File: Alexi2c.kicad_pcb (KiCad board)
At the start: 2 copper layers, 50 x 100 mm, 26 parts, among them J1 Conn_01x04, J10 Conn_01x01, J11 Conn_01x09, J12 Conn_01x02, J13 Conn_01x02, J2 Conn_02x03_Counter_Clockwise, J3 Conn_01x02, J4 Conn_01x10, J5 Conn_01x10, J6 Conn_01x09, J7 Conn_01x01, J8 Conn_01x01, J9 Conn_01x01, U1 78M05, U2 TCA9555PWR, U3 ULN2803A, U4 ULN2803A

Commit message: Readme cleanup
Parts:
- J12, J13: footprint conn_kk100:kk100_22-23-2021 -> Pin_Headers:Pin_Header_Straight_1x02_Pitch2.54mm
- moved J12 1.27 mm to (137.8, 116.2), turned to 0 degrees
- moved J13 1.27 mm to (137.8, 51.2), turned to 0 degrees

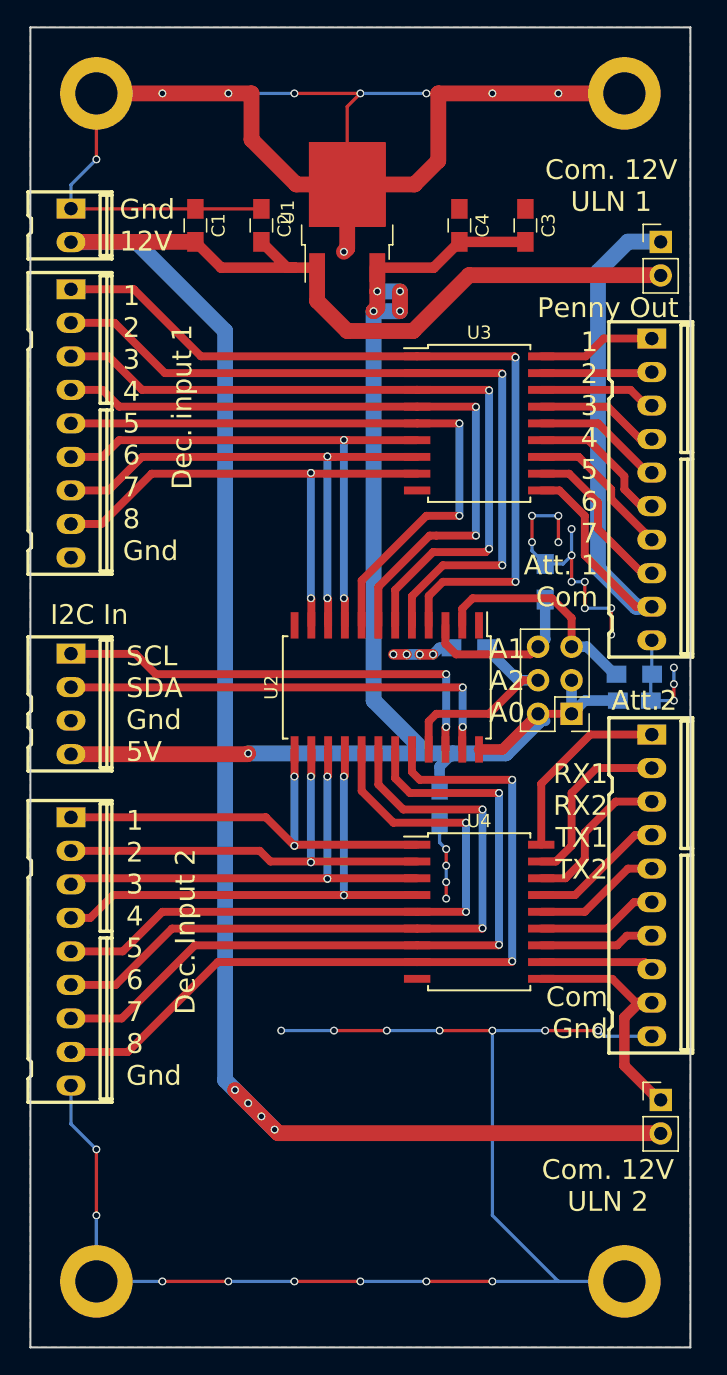
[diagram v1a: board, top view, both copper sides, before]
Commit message: new I2C decoder module
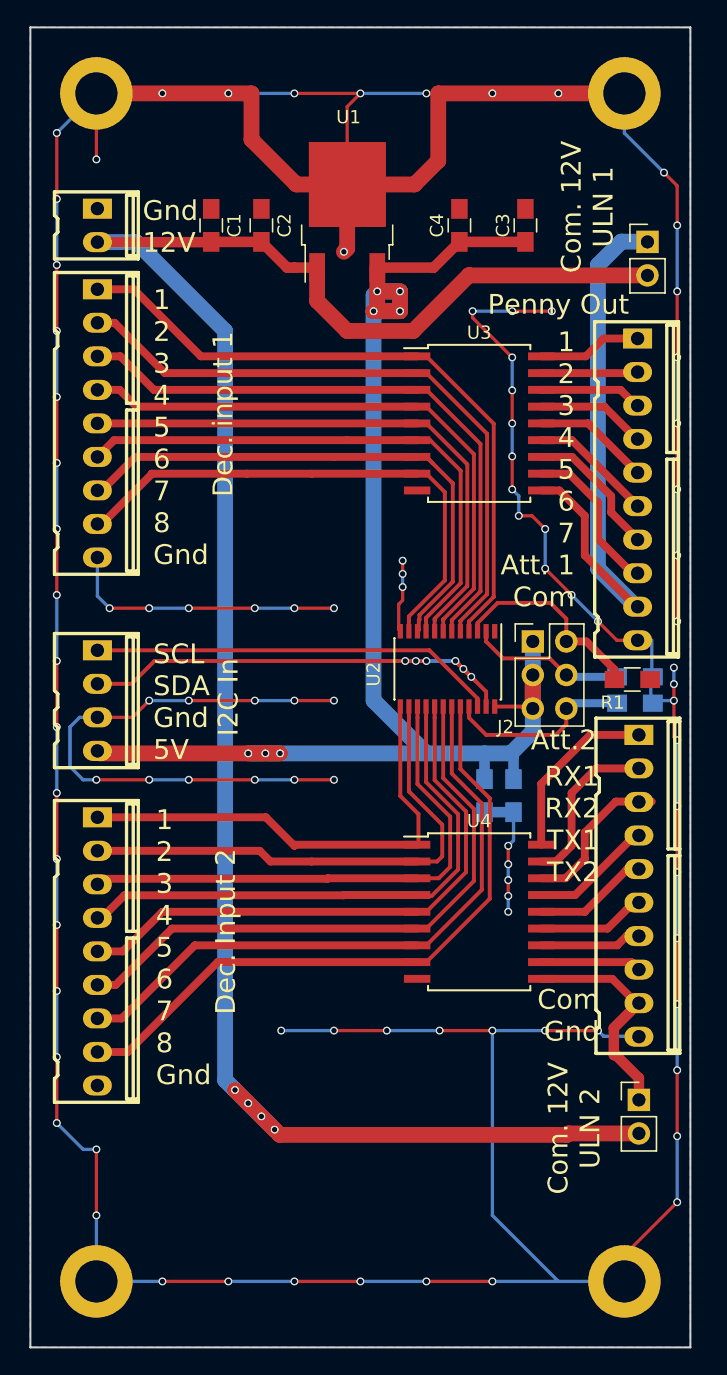
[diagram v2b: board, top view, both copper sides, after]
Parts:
- J2: value Conn_02x03_Counter_Clockwise -> Conn_02x03_Odd_Even
- R1: moved to F.Cu
- U2: footprint Housings_SOIC:SOIC-24W_7.5x15.4mm_Pitch1.27mm -> Housings_SSOP:TSSOP-24_4.4x7.8mm_Pitch0.65mm
- moved C6 13.4 mm to (124.4, 93.2), turned to 90 degrees
- moved R3 13.2 mm to (135.8, 86.2), turned to 0 degrees
- moved R1 9.92 mm to (135.6, 84.4), turned to 0 degrees
- moved J2 6.22 mm to (128.1, 81.5), turned to 0 degrees
- moved C5 5.66 mm to (126.6, 93.2)
- moved U2 4.81 mm to (121.6, 83.6)
- moved J1 2.02 mm to (95.0, 86.0)
- moved J11 2.00 mm to (95.0, 105.0)
- moved J3 2.00 mm to (95.0, 50.0)
- moved J6 2.00 mm to (95.0, 65.0)
- moved J12 1.65 mm to (136.1, 116.2)
- moved C1 1.20 mm to (103.7, 50.0)
- moved J4 1.08 mm to (135.9, 70.0)
- moved J13 1.00 mm to (136.8, 51.2)
- moved J5 0.98 mm to (136.0, 100.0)
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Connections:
- J2 pad 2: Net-(C3-Pad2) -> Net-(J2-Pad2)
- J2 pad 5: Net-(J2-Pad5) -> Net-(C3-Pad2)
- R1 pad 1: Net-(J2-Pad6) -> Net-(J2-Pad2)
- R2 pad 1: Net-(J2-Pad5) -> Net-(J2-Pad4)
- R3 pad 1: Net-(J2-Pad4) -> Net-(J2-Pad6)
- U2 pad 2: Net-(J2-Pad5) -> Net-(J2-Pad4)
- U2 pad 21: Net-(J2-Pad4) -> Net-(J2-Pad6)
- U2 pad 3: Net-(J2-Pad6) -> Net-(J2-Pad2)
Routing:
- net GND: track 272.9 -> 505.5 mm, vias 46 -> 97
- net Net-(J2-Pad5): track 16.9 -> 0.00 mm
- net Net-(J2-Pad2): track 0.00 -> 15.5 mm
- net Net-(J6-Pad1): track 62.1 -> 50.7 mm, vias 2 -> 0
- net Net-(J6-Pad2): track 58.8 -> 48.8 mm, vias 2 -> 0
- net Net-(J11-Pad8): track 59.6 -> 50.0 mm, vias 2 -> 0
- net Net-(C1-Pad2): track 165.7 -> 156.2 mm
- net Net-(J6-Pad3): track 55.8 -> 46.9 mm, vias 2 -> 0
- net Net-(J11-Pad7): track 56.7 -> 48.0 mm, vias 2 -> 0
- net Net-(J6-Pad4): track 52.9 -> 44.9 mm, vias 2 -> 0
- net Net-(J11-Pad6): track 53.3 -> 46.0 mm, vias 2 -> 0
- net Net-(J6-Pad5): track 49.3 -> 43.0 mm, vias 2 -> 0
- net Net-(J11-Pad5): track 50.0 -> 43.9 mm, vias 2 -> 0
- net Net-(J2-Pad4): track 16.6 -> 11.8 mm
- net Net-(J11-Pad4): track 38.3 -> 43.0 mm, vias 2 -> 0
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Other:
- board text added: "30/20m 60/ 40m 80m 160m 6m 12/10m 17/15m Alex LPF"
- board text removed: "30/20m 60/40m 80m 160m 6m 12/10m 17/15m Alex LPF"

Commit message: added protec. diode, I2C Pull-up, I2C Vdd strap
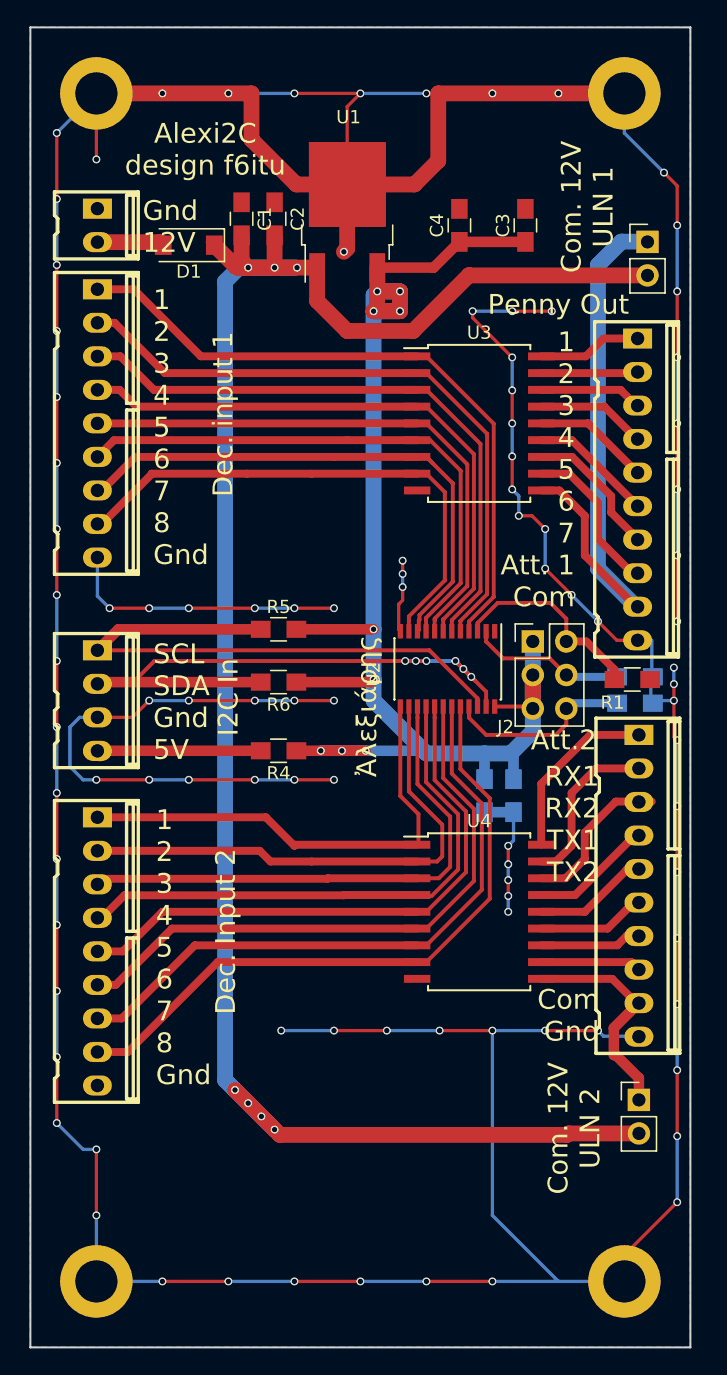
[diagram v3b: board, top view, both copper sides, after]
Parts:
- added D1: D, Diodes_SMD:D_2010, F.Cu at (102.0, 51.5)
- added R4: 0R, Resistors_SMD:R_0805_HandSoldering, F.Cu at (108.8, 89.8)
- added R5: 4k7, Resistors_SMD:R_0805_HandSoldering, F.Cu at (108.8, 80.6)
- added R6: 4k7, Resistors_SMD:R_0805_HandSoldering, F.Cu at (108.8, 84.6)
- moved C1 2.35 mm to (106.0, 49.5)
- moved C2 1.12 mm to (108.5, 49.5)
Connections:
- J1 pad 4: Net-(C3-Pad2) -> Net-(J1-Pad4)
- J3 pad 2: Net-(C1-Pad2) -> Net-(D1-Pad2)
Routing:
- net Net-(J1-Pad1): track 30.9 -> 44.0 mm
- net Net-(J1-Pad4): track 0.00 -> 12.9 mm
- net Net-(J1-Pad2): track 37.2 -> 50.0 mm
- net Net-(C1-Pad2): track 156.2 -> 150.0 mm, vias 4 -> 7
- net Net-(D1-Pad2): track 0.00 -> 5.08 mm
- net Net-(C3-Pad2): track 116.1 -> 113.8 mm, vias 7 -> 9
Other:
- board text added: "Alexi2C design f6itu"
- board text added: "Ἀλεξιάρης"

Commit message: image and BOM added, minor changes
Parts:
- removed C1: 100n, Capacitors_SMD:C_0805_HandSoldering
- removed C2: 1u, Capacitors_SMD:C_0805_HandSoldering
- removed C3, C4: C, Capacitors_SMD:C_0805_HandSoldering
- removed U1: 78M05, TO_SOT_Packages_SMD:TO-252-2
- added R7: 4k7, Resistors_SMD:R_0805_HandSoldering, F.Cu at (125.4, 77.0)
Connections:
- U2 pad 1: (no net) -> Net-(R7-Pad2)
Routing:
- net GND: track 505.5 -> 442.9 mm, vias 97 -> 96
- net Net-(C5-Pad2): track 113.8 -> 67.6 mm, vias 9 -> 4
- net Net-(D1-Pad1): track 150.0 -> 138.9 mm
- net Net-(J2-Pad2): track 15.5 -> 24.1 mm
- net Net-(R7-Pad2): track 0.00 -> 4.29 mm
- net Net-(J6-Pad6): track 42.3 -> 41.6 mm
- net Net-(J6-Pad8): track 40.2 -> 39.6 mm
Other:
- board text added: "1 2 3 4 5 6 7 Att1 Com"
- board text added: "Alexi2C f6itu"
- board text added: "Alexi2C Ἄλεξις Alexiares emulation interface"
- board text added: "Att2"
- board text removed: "1 2 3 4 5 6 7 Att. 1 Com"
- board text removed: "Alexi2C design f6itu"
- board text removed: "Att.2"

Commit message: new stitching, minor silkmask mods
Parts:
- added REF**: via, via:via, F.Cu at (139.0, 50.0)
- added REF**: via, via:via, F.Cu at (139.0, 63.5)
- added REF**: via, via:via, F.Cu at (91.0, 91.5)
- added REF**: via, via:via, F.Cu at (92.5, 90.0)
- added REF**: via, via:via, F.Cu at (91.0, 90.0)
- added REF**: via, via:via, F.Cu at (92.5, 88.5)
- added REF**: via, via:via, F.Cu at (91.0, 88.5)
- added REF**: via, via:via, F.Cu at (92.5, 87.0)
- added REF**: via, via:via, F.Cu at (91.0, 87.0)
- added REF**: via, via:via, F.Cu at (92.5, 85.5)
- added REF**: via, via:via, F.Cu at (91.0, 85.5)
- added REF**: via, via:via, F.Cu at (92.5, 84.0)
- added REF**: via, via:via, F.Cu at (139.0, 65.0)
- added REF**: via, via:via, F.Cu at (91.0, 84.0)
- added REF**: via, via:via, F.Cu at (92.5, 82.5)
- added REF**: via, via:via, F.Cu at (91.0, 82.5)
- added REF**: via, via:via, F.Cu at (92.5, 81.0)
- added REF**: via, via:via, F.Cu at (91.0, 81.0)
- added REF**: via, via:via, F.Cu at (92.5, 79.5)
- added REF**: via, via:via, F.Cu at (91.0, 79.5)
- added REF**: via, via:via, F.Cu at (92.5, 78.0)
- added REF**: via, via:via, F.Cu at (91.0, 78.0)
- added REF**: via, via:via, F.Cu at (92.5, 76.5)
- added REF**: via, via:via, F.Cu at (139.0, 66.5)
- added REF**: via, via:via, F.Cu at (91.0, 76.5)
- added REF**: via, via:via, F.Cu at (92.5, 75.0)
- added REF**: via, via:via, F.Cu at (91.0, 75.0)
- added REF**: via, via:via, F.Cu at (92.5, 73.5)
- added REF**: via, via:via, F.Cu at (91.0, 73.5)
- added REF**: via, via:via, F.Cu at (92.5, 72.0)
- added REF**: via, via:via, F.Cu at (91.0, 72.0)
- added REF**: via, via:via, F.Cu at (92.5, 70.5)
- added REF**: via, via:via, F.Cu at (91.0, 70.5)
- added REF**: via, via:via, F.Cu at (92.5, 69.0)
- added REF**: via, via:via, F.Cu at (139.0, 68.0)
- added REF**: via, via:via, F.Cu at (91.0, 69.0)
- added REF**: via, via:via, F.Cu at (92.5, 67.5)
- added REF**: via, via:via, F.Cu at (91.0, 67.5)
- added REF**: via, via:via, F.Cu at (92.5, 66.0)
- added REF**: via, via:via, F.Cu at (91.0, 66.0)
- added REF**: via, via:via, F.Cu at (92.5, 64.5)
- added REF**: via, via:via, F.Cu at (91.0, 64.5)
- added REF**: via, via:via, F.Cu at (92.5, 63.0)
- added REF**: via, via:via, F.Cu at (91.0, 63.0)
- added REF**: via, via:via, F.Cu at (92.5, 61.5)
- added REF**: via, via:via, F.Cu at (139.0, 69.5)
- added REF**: via, via:via, F.Cu at (91.0, 61.5)
- added REF**: via, via:via, F.Cu at (92.5, 60.0)
- added REF**: via, via:via, F.Cu at (91.0, 60.0)
- added REF**: via, via:via, F.Cu at (92.5, 58.5)
- added REF**: via, via:via, F.Cu at (91.0, 58.5)
- added REF**: via, via:via, F.Cu at (92.5, 57.0)
- added REF**: via, via:via, F.Cu at (91.0, 57.0)
- added REF**: via, via:via, F.Cu at (92.5, 55.5)
- added REF**: via, via:via, F.Cu at (91.0, 55.5)
- added REF**: via, via:via, F.Cu at (92.5, 54.0)
- added REF**: via, via:via, F.Cu at (139.0, 71.0)
- added REF**: via, via:via, F.Cu at (91.0, 54.0)
- added REF**: via, via:via, F.Cu at (92.5, 52.5)
- added REF**: via, via:via, F.Cu at (91.0, 52.5)
- added REF**: via, via:via, F.Cu at (92.5, 51.0)
- added REF**: via, via:via, F.Cu at (91.0, 51.0)
- added REF**: via, via:via, F.Cu at (92.5, 49.5)
- added REF**: via, via:via, F.Cu at (91.0, 49.5)
- added REF**: via, via:via, F.Cu at (92.5, 48.0)
- added REF**: via, via:via, F.Cu at (91.0, 48.0)
- added REF**: via, via:via, F.Cu at (92.5, 46.5)
- added REF**: via, via:via, F.Cu at (139.0, 72.5)
- added REF**: via, via:via, F.Cu at (91.0, 46.5)
- added REF**: via, via:via, F.Cu at (92.5, 45.0)
- added REF**: via, via:via, F.Cu at (91.0, 45.0)
- added REF**: via, via:via, F.Cu at (103.0, 76.5)
- added REF**: via, via:via, F.Cu at (101.5, 76.5)
- added REF**: via, via:via, F.Cu at (100.0, 76.5)
- added REF**: via, via:via, F.Cu at (103.0, 75.0)
- added REF**: via, via:via, F.Cu at (101.5, 75.0)
- added REF**: via, via:via, F.Cu at (100.0, 75.0)
- added REF**: via, via:via, F.Cu at (103.0, 73.5)
- added REF**: via, via:via, F.Cu at (139.0, 74.0)
- added REF**: via, via:via, F.Cu at (101.5, 73.5)
- added REF**: via, via:via, F.Cu at (100.0, 73.5)
- added REF**: via, via:via, F.Cu at (103.0, 72.0)
- added REF**: via, via:via, F.Cu at (101.5, 72.0)
- added REF**: via, via:via, F.Cu at (100.0, 72.0)
- added REF**: via, via:via, F.Cu at (108.5, 72.0)
- added REF**: via, via:via, F.Cu at (110.0, 72.0)
- added REF**: via, via:via, F.Cu at (111.5, 72.0)
- added REF**: via, via:via, F.Cu at (113.0, 72.0)
- added REF**: via, via:via, F.Cu at (114.5, 72.0)
- added REF**: via, via:via, F.Cu at (139.0, 75.5)
- added REF**: via, via:via, F.Cu at (116.0, 72.0)
- added REF**: via, via:via, F.Cu at (108.5, 73.5)
- added REF**: via, via:via, F.Cu at (110.0, 73.5)
- added REF**: via, via:via, F.Cu at (111.5, 73.5)
- added REF**: via, via:via, F.Cu at (113.0, 73.5)
- added REF**: via, via:via, F.Cu at (114.5, 73.5)
- added REF**: via, via:via, F.Cu at (116.0, 73.5)
- added REF**: via, via:via, F.Cu at (108.5, 75.0)
- added REF**: via, via:via, F.Cu at (110.0, 75.0)
- added REF**: via, via:via, F.Cu at (111.5, 75.0)
- added REF**: via, via:via, F.Cu at (139.0, 77.0)
- added REF**: via, via:via, F.Cu at (113.0, 75.0)
- added REF**: via, via:via, F.Cu at (114.5, 75.0)
- added REF**: via, via:via, F.Cu at (116.0, 75.0)
- added REF**: via, via:via, F.Cu at (108.5, 76.5)
- added REF**: via, via:via, F.Cu at (110.0, 76.5)
- added REF**: via, via:via, F.Cu at (111.5, 76.5)
- added REF**: via, via:via, F.Cu at (113.0, 76.5)
- added REF**: via, via:via, F.Cu at (114.5, 76.5)
- added REF**: via, via:via, F.Cu at (116.0, 76.5)
- added REF**: via, via:via, F.Cu at (102.5, 93.5)
- added REF**: via, via:via, F.Cu at (139.0, 51.5)
- added REF**: via, via:via, F.Cu at (139.0, 78.5)
- added REF**: via, via:via, F.Cu at (101.0, 93.5)
- added REF**: via, via:via, F.Cu at (99.5, 93.5)
- added REF**: via, via:via, F.Cu at (102.5, 92.0)
- added REF**: via, via:via, F.Cu at (101.0, 92.0)
- added REF**: via, via:via, F.Cu at (99.5, 92.0)
- added REF**: via, via:via, F.Cu at (107.5, 92.0)
- added REF**: via, via:via, F.Cu at (109.0, 92.0)
- added REF**: via, via:via, F.Cu at (110.5, 92.0)
- added REF**: via, via:via, F.Cu at (112.0, 92.0)
- added REF**: via, via:via, F.Cu at (113.5, 92.0)
- added REF**: via, via:via, F.Cu at (139.0, 80.0)
- added REF**: via, via:via, F.Cu at (115.0, 92.0)
- added REF**: via, via:via, F.Cu at (116.5, 92.0)
- added REF**: via, via:via, F.Cu at (107.5, 93.5)
- added REF**: via, via:via, F.Cu at (109.0, 93.5)
- added REF**: via, via:via, F.Cu at (110.5, 93.5)
- added REF**: via, via:via, F.Cu at (112.0, 93.5)
- added REF**: via, via:via, F.Cu at (113.5, 93.5)
- added REF**: via, via:via, F.Cu at (115.0, 93.5)
- added REF**: via, via:via, F.Cu at (116.5, 93.5)
- added REF**: via, via:via, F.Cu at (128.5, 115.0)
- added REF**: via, via:via, F.Cu at (139.0, 81.5)
- added REF**: via, via:via, F.Cu at (127.0, 115.0)
- added REF**: via, via:via, F.Cu at (125.5, 115.0)
- added REF**: via, via:via, F.Cu at (124.0, 115.0)
- added REF**: via, via:via, F.Cu at (122.5, 115.0)
- added REF**: via, via:via, F.Cu at (121.0, 115.0)
- added REF**: via, via:via, F.Cu at (119.5, 115.0)
- added REF**: via, via:via, F.Cu at (118.0, 115.0)
- added REF**: via, via:via, F.Cu at (116.5, 115.0)
- added REF**: via, via:via, F.Cu at (115.0, 115.0)
- added REF**: via, via:via, F.Cu at (113.5, 115.0)
- added REF**: via, via:via, F.Cu at (139.0, 83.0)
- added REF**: via, via:via, F.Cu at (112.0, 115.0)
- added REF**: via, via:via, F.Cu at (110.5, 115.0)
- added REF**: via, via:via, F.Cu at (109.0, 115.0)
- added REF**: via, via:via, F.Cu at (128.5, 113.5)
- added REF**: via, via:via, F.Cu at (127.0, 113.5)
- added REF**: via, via:via, F.Cu at (125.5, 113.5)
- added REF**: via, via:via, F.Cu at (124.0, 113.5)
- added REF**: via, via:via, F.Cu at (122.5, 113.5)
- added REF**: via, via:via, F.Cu at (121.0, 113.5)
- added REF**: via, via:via, F.Cu at (119.5, 113.5)
- added REF**: via, via:via, F.Cu at (139.0, 84.5)
- added REF**: via, via:via, F.Cu at (118.0, 113.5)
- added REF**: via, via:via, F.Cu at (116.5, 113.5)
- added REF**: via, via:via, F.Cu at (115.0, 113.5)
- added REF**: via, via:via, F.Cu at (113.5, 113.5)
- added REF**: via, via:via, F.Cu at (112.0, 113.5)
- added REF**: via, via:via, F.Cu at (110.5, 113.5)
- added REF**: via, via:via, F.Cu at (109.0, 113.5)
- added REF**: via, via:via, F.Cu at (128.5, 112.0)
- added REF**: via, via:via, F.Cu at (127.0, 112.0)
- added REF**: via, via:via, F.Cu at (125.5, 112.0)
- added REF**: via, via:via, F.Cu at (139.0, 86.0)
- added REF**: via, via:via, F.Cu at (124.0, 112.0)
- added REF**: via, via:via, F.Cu at (122.5, 112.0)
- added REF**: via, via:via, F.Cu at (121.0, 112.0)
- added REF**: via, via:via, F.Cu at (119.5, 112.0)
- added REF**: via, via:via, F.Cu at (118.0, 112.0)
- added REF**: via, via:via, F.Cu at (116.5, 112.0)
- added REF**: via, via:via, F.Cu at (115.0, 112.0)
- added REF**: via, via:via, F.Cu at (113.5, 112.0)
- added REF**: via, via:via, F.Cu at (112.0, 112.0)
- added REF**: via, via:via, F.Cu at (110.5, 112.0)
- added REF**: via, via:via, F.Cu at (139.0, 87.5)
- added REF**: via, via:via, F.Cu at (109.0, 112.0)
- added REF**: via, via:via, F.Cu at (128.5, 110.5)
- added REF**: via, via:via, F.Cu at (127.0, 110.5)
- added REF**: via, via:via, F.Cu at (125.5, 110.5)
- added REF**: via, via:via, F.Cu at (124.0, 110.5)
- added REF**: via, via:via, F.Cu at (122.5, 110.5)
- added REF**: via, via:via, F.Cu at (121.0, 110.5)
- added REF**: via, via:via, F.Cu at (119.5, 110.5)
- added REF**: via, via:via, F.Cu at (118.0, 110.5)
- added REF**: via, via:via, F.Cu at (116.5, 110.5)
- added REF**: via, via:via, F.Cu at (139.0, 89.0)
- added REF**: via, via:via, F.Cu at (115.0, 110.5)
- added REF**: via, via:via, F.Cu at (113.5, 110.5)
- added REF**: via, via:via, F.Cu at (112.0, 110.5)
- added REF**: via, via:via, F.Cu at (110.5, 110.5)
- added REF**: via, via:via, F.Cu at (109.0, 110.5)
- added REF**: via, via:via, F.Cu at (99.0, 129.0)
- added REF**: via, via:via, F.Cu at (100.5, 129.0)
- added REF**: via, via:via, F.Cu at (102.0, 129.0)
- added REF**: via, via:via, F.Cu at (103.5, 129.0)
- added REF**: via, via:via, F.Cu at (105.0, 129.0)
- added REF**: via, via:via, F.Cu at (139.0, 90.5)
- added REF**: via, via:via, F.Cu at (106.5, 129.0)
- added REF**: via, via:via, F.Cu at (108.0, 129.0)
- added REF**: via, via:via, F.Cu at (109.5, 129.0)
- added REF**: via, via:via, F.Cu at (111.0, 129.0)
- added REF**: via, via:via, F.Cu at (112.5, 129.0)
- added REF**: via, via:via, F.Cu at (114.0, 129.0)
- added REF**: via, via:via, F.Cu at (115.5, 129.0)
- added REF**: via, via:via, F.Cu at (117.0, 129.0)
- added REF**: via, via:via, F.Cu at (118.5, 129.0)
- added REF**: via, via:via, F.Cu at (120.0, 129.0)
- added REF**: via, via:via, F.Cu at (139.0, 92.0)
- added REF**: via, via:via, F.Cu at (121.5, 129.0)
- added REF**: via, via:via, F.Cu at (123.0, 129.0)
- added REF**: via, via:via, F.Cu at (124.5, 129.0)
- added REF**: via, via:via, F.Cu at (126.0, 129.0)
- added REF**: via, via:via, F.Cu at (127.5, 129.0)
- added REF**: via, via:via, F.Cu at (129.0, 129.0)
- added REF**: via, via:via, F.Cu at (130.5, 129.0)
- added REF**: via, via:via, F.Cu at (99.0, 130.5)
- added REF**: via, via:via, F.Cu at (100.5, 130.5)
- added REF**: via, via:via, F.Cu at (102.0, 130.5)
- added REF**: via, via:via, F.Cu at (139.0, 53.0)
- added REF**: via, via:via, F.Cu at (139.0, 93.5)
- added REF**: via, via:via, F.Cu at (103.5, 130.5)
- added REF**: via, via:via, F.Cu at (105.0, 130.5)
- added REF**: via, via:via, F.Cu at (106.5, 130.5)
- added REF**: via, via:via, F.Cu at (108.0, 130.5)
- added REF**: via, via:via, F.Cu at (109.5, 130.5)
- added REF**: via, via:via, F.Cu at (111.0, 130.5)
- added REF**: via, via:via, F.Cu at (112.5, 130.5)
- added REF**: via, via:via, F.Cu at (114.0, 130.5)
- added REF**: via, via:via, F.Cu at (115.5, 130.5)
- added REF**: via, via:via, F.Cu at (117.0, 130.5)
- added REF**: via, via:via, F.Cu at (139.0, 95.0)
- added REF**: via, via:via, F.Cu at (118.5, 130.5)
- added REF**: via, via:via, F.Cu at (120.0, 130.5)
- added REF**: via, via:via, F.Cu at (121.5, 130.5)
- added REF**: via, via:via, F.Cu at (123.0, 130.5)
- added REF**: via, via:via, F.Cu at (124.5, 130.5)
- added REF**: via, via:via, F.Cu at (126.0, 130.5)
- added REF**: via, via:via, F.Cu at (127.5, 130.5)
- added REF**: via, via:via, F.Cu at (129.0, 130.5)
- added REF**: via, via:via, F.Cu at (130.5, 130.5)
- added REF**: via, via:via, F.Cu at (99.0, 132.0)
- added REF**: via, via:via, F.Cu at (139.0, 96.5)
- added REF**: via, via:via, F.Cu at (100.5, 132.0)
- added REF**: via, via:via, F.Cu at (102.0, 132.0)
- added REF**: via, via:via, F.Cu at (103.5, 132.0)
- added REF**: via, via:via, F.Cu at (105.0, 132.0)
- added REF**: via, via:via, F.Cu at (106.5, 132.0)
- added REF**: via, via:via, F.Cu at (108.0, 132.0)
- added REF**: via, via:via, F.Cu at (109.5, 132.0)
- added REF**: via, via:via, F.Cu at (111.0, 132.0)
- added REF**: via, via:via, F.Cu at (112.5, 132.0)
- added REF**: via, via:via, F.Cu at (114.0, 132.0)
- added REF**: via, via:via, F.Cu at (139.0, 98.0)
- added REF**: via, via:via, F.Cu at (115.5, 132.0)
- added REF**: via, via:via, F.Cu at (117.0, 132.0)
- added REF**: via, via:via, F.Cu at (118.5, 132.0)
- added REF**: via, via:via, F.Cu at (120.0, 132.0)
- added REF**: via, via:via, F.Cu at (121.5, 132.0)
- added REF**: via, via:via, F.Cu at (123.0, 132.0)
- added REF**: via, via:via, F.Cu at (124.5, 132.0)
- added REF**: via, via:via, F.Cu at (126.0, 132.0)
- added REF**: via, via:via, F.Cu at (127.5, 132.0)
- added REF**: via, via:via, F.Cu at (129.0, 132.0)
- added REF**: via, via:via, F.Cu at (139.0, 99.5)
- added REF**: via, via:via, F.Cu at (130.5, 132.0)
- added REF**: via, via:via, F.Cu at (99.0, 133.5)
- added REF**: via, via:via, F.Cu at (100.5, 133.5)
- added REF**: via, via:via, F.Cu at (102.0, 133.5)
- added REF**: via, via:via, F.Cu at (103.5, 133.5)
- added REF**: via, via:via, F.Cu at (105.0, 133.5)
- added REF**: via, via:via, F.Cu at (106.5, 133.5)
- added REF**: via, via:via, F.Cu at (108.0, 133.5)
- added REF**: via, via:via, F.Cu at (109.5, 133.5)
- added REF**: via, via:via, F.Cu at (111.0, 133.5)
- added REF**: via, via:via, F.Cu at (139.0, 101.0)
- added REF**: via, via:via, F.Cu at (112.5, 133.5)
- added REF**: via, via:via, F.Cu at (114.0, 133.5)
- added REF**: via, via:via, F.Cu at (115.5, 133.5)
- added REF**: via, via:via, F.Cu at (117.0, 133.5)
- added REF**: via, via:via, F.Cu at (118.5, 133.5)
- added REF**: via, via:via, F.Cu at (120.0, 133.5)
- added REF**: via, via:via, F.Cu at (121.5, 133.5)
- added REF**: via, via:via, F.Cu at (123.0, 133.5)
- added REF**: via, via:via, F.Cu at (124.5, 133.5)
- added REF**: via, via:via, F.Cu at (126.0, 133.5)
- added REF**: via, via:via, F.Cu at (139.0, 102.5)
- added REF**: via, via:via, F.Cu at (127.5, 133.5)
- added REF**: via, via:via, F.Cu at (129.0, 133.5)
- added REF**: via, via:via, F.Cu at (130.5, 133.5)
- added REF**: via, via:via, F.Cu at (130.5, 40.5)
- added REF**: via, via:via, F.Cu at (129.0, 40.5)
- added REF**: via, via:via, F.Cu at (127.5, 40.5)
- added REF**: via, via:via, F.Cu at (126.0, 40.5)
- added REF**: via, via:via, F.Cu at (124.5, 40.5)
- added REF**: via, via:via, F.Cu at (123.0, 40.5)
- added REF**: via, via:via, F.Cu at (121.5, 40.5)
- added REF**: via, via:via, F.Cu at (139.0, 104.0)
- added REF**: via, via:via, F.Cu at (120.0, 40.5)
- added REF**: via, via:via, F.Cu at (118.5, 40.5)
- added REF**: via, via:via, F.Cu at (117.0, 40.5)
- added REF**: via, via:via, F.Cu at (115.5, 40.5)
- added REF**: via, via:via, F.Cu at (114.0, 40.5)
- added REF**: via, via:via, F.Cu at (112.5, 40.5)
- added REF**: via, via:via, F.Cu at (111.0, 40.5)
- added REF**: via, via:via, F.Cu at (109.5, 40.5)
- added REF**: via, via:via, F.Cu at (108.0, 40.5)
- added REF**: via, via:via, F.Cu at (106.5, 40.5)
- added REF**: via, via:via, F.Cu at (139.0, 105.5)
- added REF**: via, via:via, F.Cu at (105.0, 40.5)
- added REF**: via, via:via, F.Cu at (103.5, 40.5)
- added REF**: via, via:via, F.Cu at (102.0, 40.5)
- added REF**: via, via:via, F.Cu at (100.5, 40.5)
- added REF**: via, via:via, F.Cu at (99.0, 40.5)
- added REF**: via, via:via, F.Cu at (130.5, 39.0)
- added REF**: via, via:via, F.Cu at (129.0, 39.0)
- added REF**: via, via:via, F.Cu at (127.5, 39.0)
- added REF**: via, via:via, F.Cu at (126.0, 39.0)
- added REF**: via, via:via, F.Cu at (124.5, 39.0)
- added REF**: via, via:via, F.Cu at (139.0, 107.0)
- added REF**: via, via:via, F.Cu at (123.0, 39.0)
- added REF**: via, via:via, F.Cu at (121.5, 39.0)
- added REF**: via, via:via, F.Cu at (120.0, 39.0)
- added REF**: via, via:via, F.Cu at (118.5, 39.0)
- added REF**: via, via:via, F.Cu at (117.0, 39.0)
- added REF**: via, via:via, F.Cu at (115.5, 39.0)
- added REF**: via, via:via, F.Cu at (114.0, 39.0)
- added REF**: via, via:via, F.Cu at (112.5, 39.0)
- added REF**: via, via:via, F.Cu at (111.0, 39.0)
- added REF**: via, via:via, F.Cu at (109.5, 39.0)
- added REF**: via, via:via, F.Cu at (139.0, 54.5)
- added REF**: via, via:via, F.Cu at (139.0, 108.5)
- added REF**: via, via:via, F.Cu at (108.0, 39.0)
- added REF**: via, via:via, F.Cu at (106.5, 39.0)
- added REF**: via, via:via, F.Cu at (105.0, 39.0)
- added REF**: via, via:via, F.Cu at (103.5, 39.0)
- added REF**: via, via:via, F.Cu at (102.0, 39.0)
- added REF**: via, via:via, F.Cu at (100.5, 39.0)
- added REF**: via, via:via, F.Cu at (99.0, 39.0)
- added REF**: via, via:via, F.Cu at (130.5, 37.5)
- added REF**: via, via:via, F.Cu at (129.0, 37.5)
- added REF**: via, via:via, F.Cu at (127.5, 37.5)
- added REF**: via, via:via, F.Cu at (139.0, 110.0)
- added REF**: via, via:via, F.Cu at (126.0, 37.5)
- added REF**: via, via:via, F.Cu at (124.5, 37.5)
- added REF**: via, via:via, F.Cu at (123.0, 37.5)
- added REF**: via, via:via, F.Cu at (121.5, 37.5)
- added REF**: via, via:via, F.Cu at (120.0, 37.5)
- added REF**: via, via:via, F.Cu at (118.5, 37.5)
- added REF**: via, via:via, F.Cu at (117.0, 37.5)
- added REF**: via, via:via, F.Cu at (115.5, 37.5)
- added REF**: via, via:via, F.Cu at (114.0, 37.5)
- added REF**: via, via:via, F.Cu at (112.5, 37.5)
- added REF**: via, via:via, F.Cu at (139.0, 111.5)
- added REF**: via, via:via, F.Cu at (111.0, 37.5)
- added REF**: via, via:via, F.Cu at (109.5, 37.5)
- added REF**: via, via:via, F.Cu at (108.0, 37.5)
- added REF**: via, via:via, F.Cu at (106.5, 37.5)
- added REF**: via, via:via, F.Cu at (105.0, 37.5)
- added REF**: via, via:via, F.Cu at (103.5, 37.5)
- added REF**: via, via:via, F.Cu at (102.0, 37.5)
- added REF**: via, via:via, F.Cu at (100.5, 37.5)
- added REF**: via, via:via, F.Cu at (99.0, 37.5)
- added REF**: via, via:via, F.Cu at (130.5, 36.0)
- added REF**: via, via:via, F.Cu at (139.0, 113.0)
- added REF**: via, via:via, F.Cu at (129.0, 36.0)
- added REF**: via, via:via, F.Cu at (127.5, 36.0)
- added REF**: via, via:via, F.Cu at (126.0, 36.0)
- added REF**: via, via:via, F.Cu at (124.5, 36.0)
- added REF**: via, via:via, F.Cu at (123.0, 36.0)
- added REF**: via, via:via, F.Cu at (121.5, 36.0)
- added REF**: via, via:via, F.Cu at (120.0, 36.0)
- added REF**: via, via:via, F.Cu at (118.5, 36.0)
- added REF**: via, via:via, F.Cu at (117.0, 36.0)
- added REF**: via, via:via, F.Cu at (115.5, 36.0)
- added REF**: via, via:via, F.Cu at (139.0, 114.5)
- added REF**: via, via:via, F.Cu at (114.0, 36.0)
- added REF**: via, via:via, F.Cu at (112.5, 36.0)
- added REF**: via, via:via, F.Cu at (111.0, 36.0)
- added REF**: via, via:via, F.Cu at (109.5, 36.0)
- added REF**: via, via:via, F.Cu at (108.0, 36.0)
- added REF**: via, via:via, F.Cu at (106.5, 36.0)
- added REF**: via, via:via, F.Cu at (105.0, 36.0)
- added REF**: via, via:via, F.Cu at (103.5, 36.0)
- added REF**: via, via:via, F.Cu at (102.0, 36.0)
- added REF**: via, via:via, F.Cu at (100.5, 36.0)
- added REF**: via, via:via, F.Cu at (139.0, 116.0)
- added REF**: via, via:via, F.Cu at (99.0, 36.0)
- added REF**: via, via:via, F.Cu at (139.0, 117.5)
- added REF**: via, via:via, F.Cu at (139.0, 119.0)
- added REF**: via, via:via, F.Cu at (139.0, 120.5)
- added REF**: via, via:via, F.Cu at (139.0, 122.0)
- added REF**: via, via:via, F.Cu at (139.0, 56.0)
- added REF**: via, via:via, F.Cu at (139.0, 123.5)
- added REF**: via, via:via, F.Cu at (139.0, 125.0)
- added REF**: via, via:via, F.Cu at (139.0, 126.5)
- added REF**: via, via:via, F.Cu at (139.0, 128.0)
- added REF**: via, via:via, F.Cu at (139.0, 129.5)
- added REF**: via, via:via, F.Cu at (92.5, 124.5)
- added REF**: via, via:via, F.Cu at (91.0, 124.5)
- added REF**: via, via:via, F.Cu at (92.5, 123.0)
- added REF**: via, via:via, F.Cu at (91.0, 123.0)
- added REF**: via, via:via, F.Cu at (92.5, 121.5)
- added REF**: via, via:via, F.Cu at (139.0, 57.5)
- added REF**: via, via:via, F.Cu at (91.0, 121.5)
- added REF**: via, via:via, F.Cu at (92.5, 120.0)
- added REF**: via, via:via, F.Cu at (91.0, 120.0)
- added REF**: via, via:via, F.Cu at (92.5, 118.5)
- added REF**: via, via:via, F.Cu at (91.0, 118.5)
- added REF**: via, via:via, F.Cu at (92.5, 117.0)
- added REF**: via, via:via, F.Cu at (91.0, 117.0)
- added REF**: via, via:via, F.Cu at (92.5, 115.5)
- added REF**: via, via:via, F.Cu at (91.0, 115.5)
- added REF**: via, via:via, F.Cu at (92.5, 114.0)
- added REF**: via, via:via, F.Cu at (139.0, 59.0)
- added REF**: via, via:via, F.Cu at (91.0, 114.0)
- added REF**: via, via:via, F.Cu at (92.5, 112.5)
- added REF**: via, via:via, F.Cu at (91.0, 112.5)
- added REF**: via, via:via, F.Cu at (92.5, 111.0)
- added REF**: via, via:via, F.Cu at (91.0, 111.0)
- added REF**: via, via:via, F.Cu at (92.5, 109.5)
- added REF**: via, via:via, F.Cu at (91.0, 109.5)
- added REF**: via, via:via, F.Cu at (92.5, 108.0)
- added REF**: via, via:via, F.Cu at (91.0, 108.0)
- added REF**: via, via:via, F.Cu at (92.5, 106.5)
- added REF**: via, via:via, F.Cu at (139.0, 60.5)
- added REF**: via, via:via, F.Cu at (91.0, 106.5)
- added REF**: via, via:via, F.Cu at (92.5, 105.0)
- added REF**: via, via:via, F.Cu at (91.0, 105.0)
- added REF**: via, via:via, F.Cu at (92.5, 103.5)
- added REF**: via, via:via, F.Cu at (91.0, 103.5)
- added REF**: via, via:via, F.Cu at (92.5, 102.0)
- added REF**: via, via:via, F.Cu at (91.0, 102.0)
- added REF**: via, via:via, F.Cu at (92.5, 100.5)
- added REF**: via, via:via, F.Cu at (91.0, 100.5)
- added REF**: via, via:via, F.Cu at (92.5, 99.0)
- added REF**: via, via:via, F.Cu at (139.0, 62.0)
- added REF**: via, via:via, F.Cu at (91.0, 99.0)
- added REF**: via, via:via, F.Cu at (92.5, 97.5)
- added REF**: via, via:via, F.Cu at (91.0, 97.5)
- added REF**: via, via:via, F.Cu at (92.5, 96.0)
- added REF**: via, via:via, F.Cu at (91.0, 96.0)
- added REF**: via, via:via, F.Cu at (92.5, 94.5)
- added REF**: via, via:via, F.Cu at (91.0, 94.5)
- added REF**: via, via:via, F.Cu at (92.5, 93.0)
- added REF**: via, via:via, F.Cu at (91.0, 93.0)
- added REF**: via, via:via, F.Cu at (92.5, 91.5)
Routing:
- net GND: track 442.9 -> 90.7 mm, vias 96 -> 26
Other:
- board text added: "Alexi2C V2.0 f6itu"
- board text removed: "Alexi2C f6itu"

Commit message: Alexi2C V2.0 RTM
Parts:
- removed J7: Conn_01x01, Mounting_Holes:MountingHole_3.2mm_M3_ISO14580_Pad
- removed the REF** at (92.5, 90.0)
- removed the REF** at (92.5, 88.5)
- removed the REF** at (92.5, 87.0)
- removed the REF** at (92.5, 85.5)
- removed the REF** at (92.5, 84.0)
- removed the REF** at (92.5, 82.5)
- removed the REF** at (92.5, 81.0)
- removed the REF** at (92.5, 79.5)
- removed the REF** at (92.5, 78.0)
- removed the REF** at (92.5, 76.5)
- removed the REF** at (92.5, 75.0)
- removed the REF** at (92.5, 73.5)
- removed the REF** at (92.5, 72.0)
- removed the REF** at (92.5, 70.5)
- removed the REF** at (92.5, 69.0)
- removed the REF** at (92.5, 67.5)
- removed the REF** at (92.5, 66.0)
- removed the REF** at (92.5, 64.5)
- removed the REF** at (92.5, 63.0)
- removed the REF** at (92.5, 61.5)
- removed the REF** at (92.5, 60.0)
- removed the REF** at (92.5, 58.5)
- removed the REF** at (92.5, 57.0)
- removed the REF** at (92.5, 55.5)
- removed the REF** at (92.5, 54.0)
- removed the REF** at (92.5, 52.5)
- removed the REF** at (92.5, 51.0)
- removed the REF** at (92.5, 49.5)
- removed the REF** at (92.5, 48.0)
- removed the REF** at (92.5, 46.5)
- removed the REF** at (92.5, 45.0)
- removed the REF** at (99.0, 129.0)
- removed the REF** at (100.5, 129.0)
- removed the REF** at (102.0, 129.0)
- removed the REF** at (103.5, 129.0)
- removed the REF** at (105.0, 129.0)
- removed the REF** at (106.5, 129.0)
- removed the REF** at (108.0, 129.0)
- removed the REF** at (109.5, 129.0)
- removed the REF** at (111.0, 129.0)
- removed the REF** at (112.5, 129.0)
- removed the REF** at (114.0, 129.0)
- removed the REF** at (115.5, 129.0)
- removed the REF** at (117.0, 129.0)
- removed the REF** at (118.5, 129.0)
- removed the REF** at (120.0, 129.0)
- removed the REF** at (121.5, 129.0)
- removed the REF** at (123.0, 129.0)
- removed the REF** at (124.5, 129.0)
- removed the REF** at (126.0, 129.0)
- removed the REF** at (127.5, 129.0)
- removed the REF** at (129.0, 129.0)
- removed the REF** at (130.5, 129.0)
- removed the REF** at (99.0, 133.5)
- removed the REF** at (100.5, 133.5)
- removed the REF** at (102.0, 133.5)
- removed the REF** at (103.5, 133.5)
- removed the REF** at (105.0, 133.5)
- removed the REF** at (106.5, 133.5)
- removed the REF** at (108.0, 133.5)
- removed the REF** at (109.5, 133.5)
- removed the REF** at (111.0, 133.5)
- removed the REF** at (112.5, 133.5)
- removed the REF** at (114.0, 133.5)
- removed the REF** at (115.5, 133.5)
- removed the REF** at (117.0, 133.5)
- removed the REF** at (118.5, 133.5)
- removed the REF** at (120.0, 133.5)
- removed the REF** at (121.5, 133.5)
- removed the REF** at (123.0, 133.5)
- removed the REF** at (124.5, 133.5)
- removed the REF** at (126.0, 133.5)
- removed the REF** at (127.5, 133.5)
- removed the REF** at (129.0, 133.5)
- removed the REF** at (130.5, 133.5)
- removed the REF** at (130.5, 40.5)
- removed the REF** at (129.0, 40.5)
- removed the REF** at (127.5, 40.5)
- removed the REF** at (126.0, 40.5)
- removed the REF** at (124.5, 40.5)
- removed the REF** at (123.0, 40.5)
- removed the REF** at (121.5, 40.5)
- removed the REF** at (120.0, 40.5)
- removed the REF** at (118.5, 40.5)
- removed the REF** at (117.0, 40.5)
- removed the REF** at (115.5, 40.5)
- removed the REF** at (114.0, 40.5)
- removed the REF** at (112.5, 40.5)
- removed the REF** at (111.0, 40.5)
- removed the REF** at (109.5, 40.5)
- removed the REF** at (108.0, 40.5)
- removed the REF** at (106.5, 40.5)
- removed the REF** at (105.0, 40.5)
- removed the REF** at (103.5, 40.5)
- removed the REF** at (102.0, 40.5)
- removed the REF** at (100.5, 40.5)
- removed the REF** at (99.0, 40.5)
- removed the REF** at (130.5, 36.0)
- removed the REF** at (129.0, 36.0)
- removed the REF** at (127.5, 36.0)
- removed the REF** at (126.0, 36.0)
- removed the REF** at (124.5, 36.0)
- removed the REF** at (123.0, 36.0)
- removed the REF** at (121.5, 36.0)
- removed the REF** at (120.0, 36.0)
- removed the REF** at (118.5, 36.0)
- removed the REF** at (117.0, 36.0)
- removed the REF** at (115.5, 36.0)
- removed the REF** at (114.0, 36.0)
- removed the REF** at (112.5, 36.0)
- removed the REF** at (111.0, 36.0)
- removed the REF** at (109.5, 36.0)
- removed the REF** at (108.0, 36.0)
- removed the REF** at (106.5, 36.0)
- removed the REF** at (105.0, 36.0)
- removed the REF** at (103.5, 36.0)
- removed the REF** at (102.0, 36.0)
- removed the REF** at (100.5, 36.0)
- removed the REF** at (99.0, 36.0)
- removed the REF** at (92.5, 124.5)
- removed the REF** at (92.5, 123.0)
- removed the REF** at (92.5, 121.5)
- removed the REF** at (92.5, 120.0)
- removed the REF** at (92.5, 118.5)
- removed the REF** at (92.5, 117.0)
- removed the REF** at (92.5, 115.5)
- removed the REF** at (92.5, 114.0)
- removed the REF** at (92.5, 112.5)
- removed the REF** at (92.5, 111.0)
- removed the REF** at (92.5, 109.5)
- removed the REF** at (92.5, 108.0)
- removed the REF** at (92.5, 106.5)
- removed the REF** at (92.5, 105.0)
- removed the REF** at (92.5, 103.5)
- removed the REF** at (92.5, 102.0)
- removed the REF** at (92.5, 100.5)
- removed the REF** at (92.5, 99.0)
- removed the REF** at (92.5, 97.5)
- removed the REF** at (92.5, 96.0)
- removed the REF** at (92.5, 94.5)
- removed the REF** at (92.5, 91.5)
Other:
- board text added: "1 2 3 4 5 6 7 8 Com"
- board text added: "9 10 11 12 13 14 15 16 Com Gnd"
- board text added: "A2 A1 A0"
- board text added: "Alexi2C Ἄλεξις I2C interface"
- board text added: "Out"
- board text added: "SCL SDA Gnd Vcc"
- board text removed: "1 2 3 4 5 6 7 Att1 Com"
- board text removed: "30/20m 60/ 40m 80m 160m 6m 12/10m 17/15m Alex LPF"
- board text removed: "A1 A2 A0"
- board text removed: "Alex HPF 13 MHz 20 MHz 9.5 MHz 6.5 MHz 1.5 MHz ByPass LNA On/Off T/R Disable"
- board text removed: "Alexi2C Ἄλεξις Alexiares emulation interface"
- board text removed: "Att2"
- board text removed: "Penny Out"
- board text removed: "RX1 RX2 TX1 TX2 Com Gnd"
- board text removed: "SCL SDA Gnd 5V"
